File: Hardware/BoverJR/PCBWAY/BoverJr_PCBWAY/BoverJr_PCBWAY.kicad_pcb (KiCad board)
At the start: 2 copper layers, 100 x 100 mm, 55 parts, among them J1 Encoder Derecho, J10 7.4v, J11 Cable_PAD, J2 Encoder Izquierdo, J3 Programador, J4 Distancia_Der, J5 Distancia_Izq, J6 Cable_PAD, J7 Cable_PAD, J8 Distancia_Frontal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

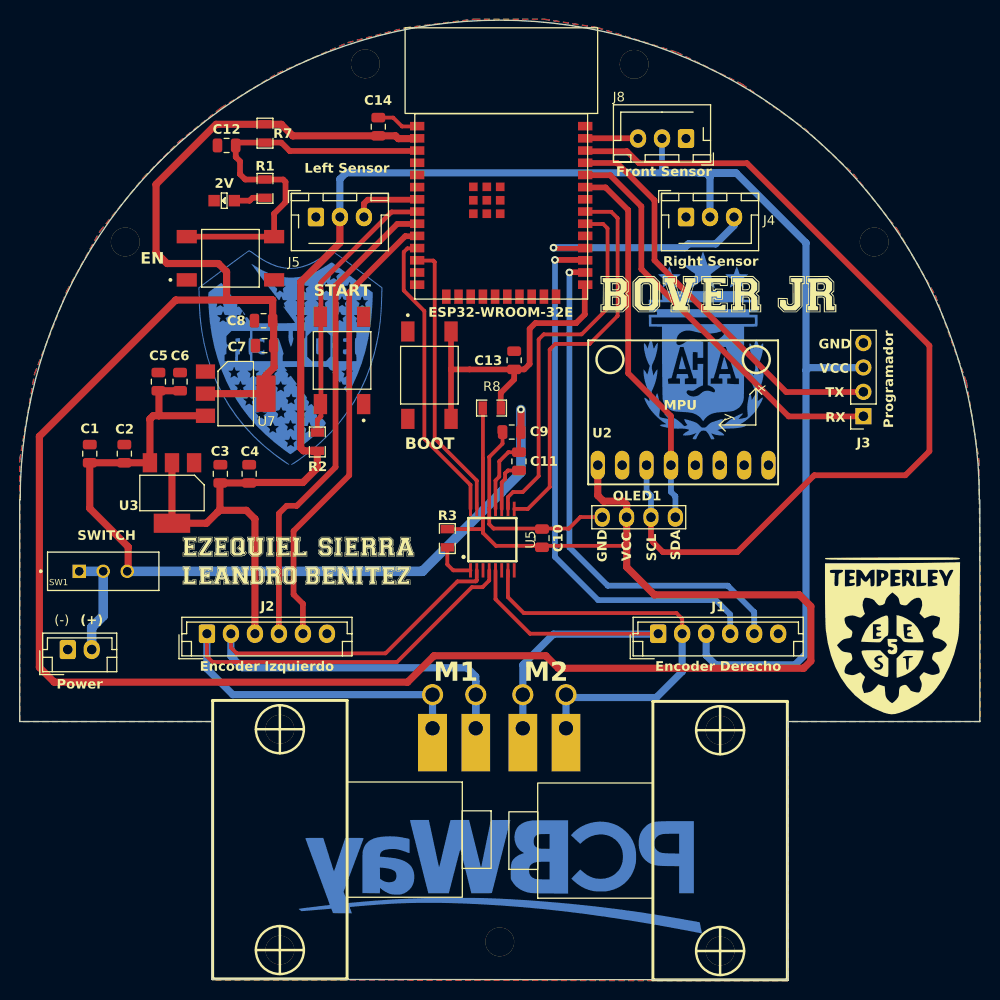
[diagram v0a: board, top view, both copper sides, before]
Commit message: AÑADI BOTON A LABERINTO CHASIS PLACA
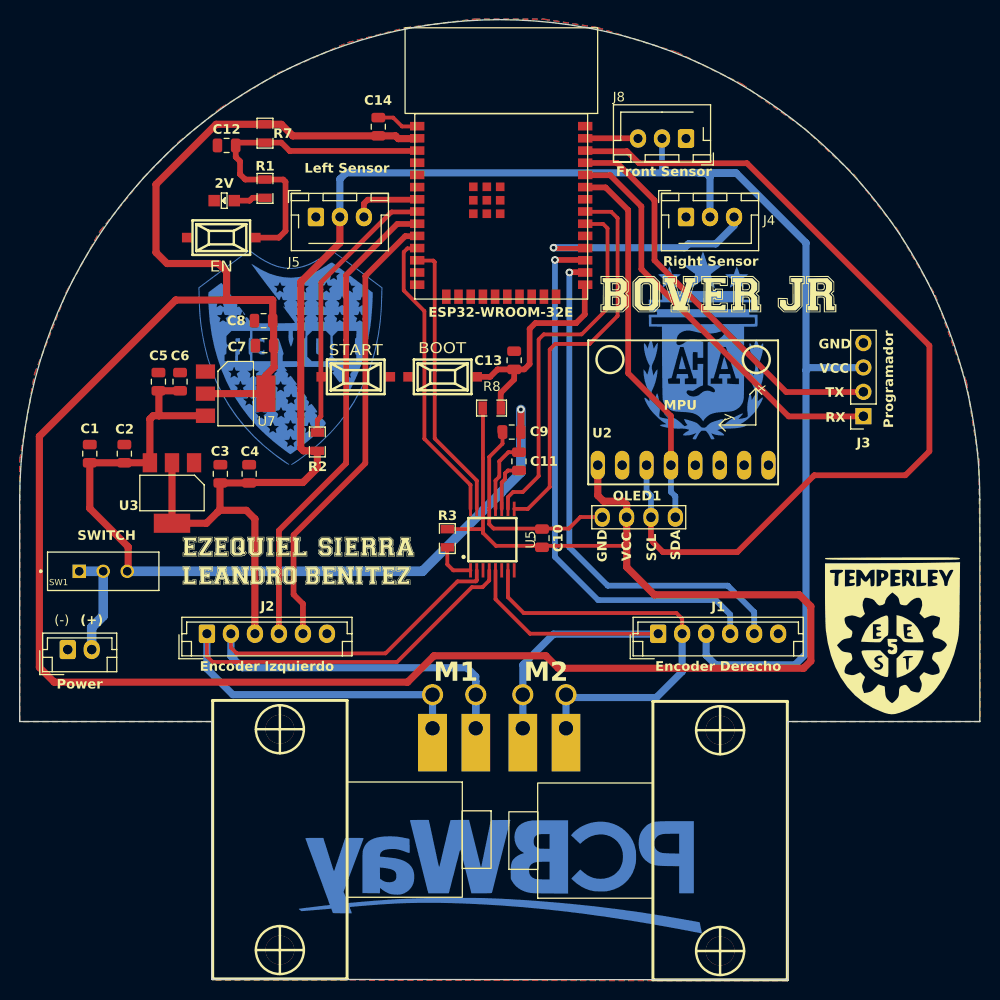
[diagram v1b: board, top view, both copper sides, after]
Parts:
- removed ? (x5): , 
- SW_BOOT1, SW_EN1, SW_START1: footprint EESTN5:SW_TL3301FF160QG -> EESTN5:Pulsador_SMD_2_BAJO
- moved SW_EN1 2.35 mm to (121.0, 52.5)
- moved SW_START1 2.23 mm to (135.0, 67.0), turned to 180 degrees
- moved SW_BOOT1 1.39 mm to (144.1, 67.0), turned to 0 degrees
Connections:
- SW_BOOT1 pad 2: GND -> /BOOT
- SW_EN1 pad 2: GND -> /EN
- SW_START1 pad 2: GND -> /START
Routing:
- net /BOOT: track 35.3 -> 23.8 mm
- net /EN: track 42.9 -> 36.1 mm
- net /OUT_M2_DA: track 50.5 -> 49.9 mm
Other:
- outline, holes or cut-outs redrawn

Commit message: corregi pcb bover JR
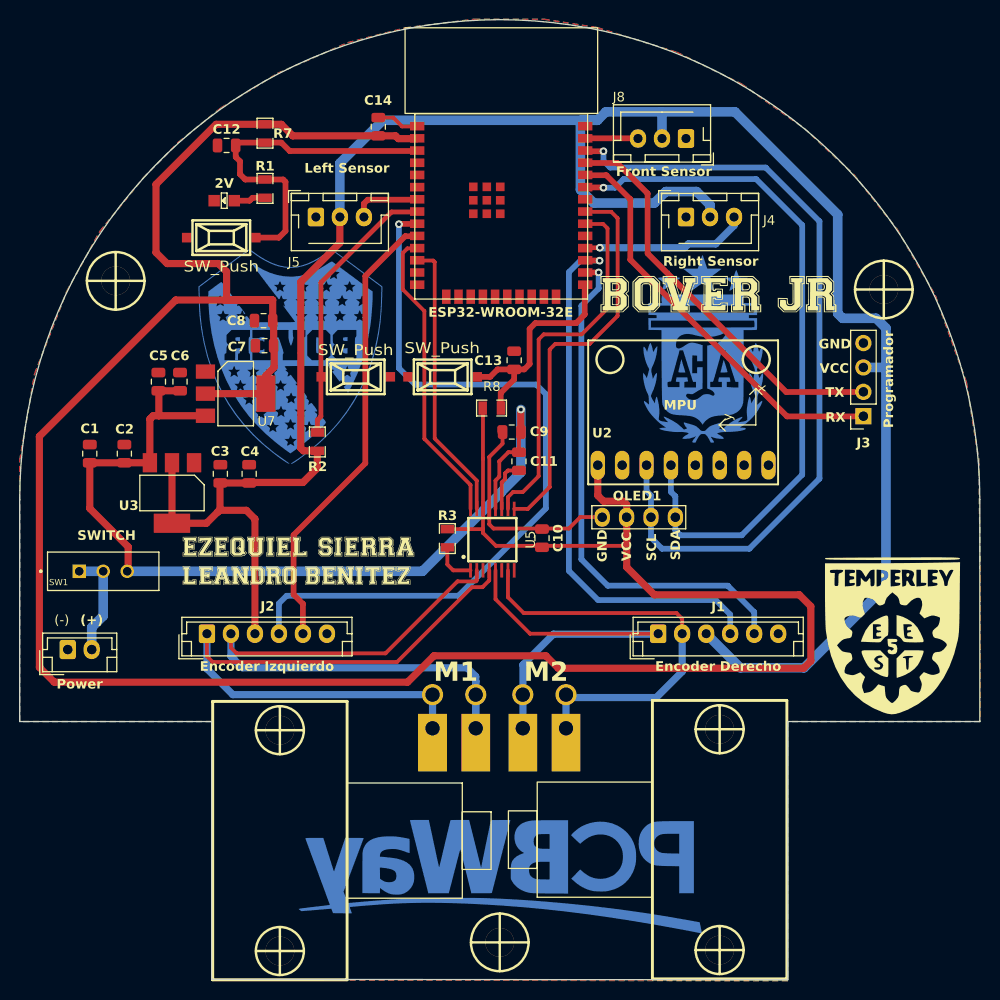
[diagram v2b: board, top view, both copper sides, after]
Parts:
- added H3: Mounting_Hole, EESTN5:hole_3mm, F.Cu at (150.0, 125.9)
- added H4: Mounting_Hole, EESTN5:hole_3mm, F.Cu at (190.0, 57.9)
- added H5: Mounting_Hole, EESTN5:hole_3mm, F.Cu at (110.0, 57.0)
- G2: footprint EESTN5:Bover_Huella_frontal_FCU -> EESTN5:Bover_Huella_BCU_SOLK
- G3: footprint EESTN5:AFA -> EESTN5:AFA_BCU_filks
- SW_BOOT1: value BOOT -> SW_Push
- SW_EN1: value EN -> SW_Push
- SW_START1: value START -> SW_Push
- moved H2 45.8 mm to (127.1, 115.3), turned to -90 degrees
- moved H1 45.8 mm to (172.9, 115.2), turned to 90 degrees
- moved G3 0.35 mm to (171.1, 64.2)
- moved G2 0.10 mm to (128.4, 64.4)
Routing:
- net /SDA: track 39.5 -> 74.0 mm, vias 0 -> 1
- net /OUT_M2_DA: track 49.9 -> 80.3 mm, vias 0 -> 1
- net +5V: track 201.9 -> 232.3 mm
- net /SCL: track 97.1 -> 83.6 mm, vias 0 -> 1
- net /IR_IZQ: track 24.0 -> 17.4 mm

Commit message: laberinto bover JR falta estañar logos
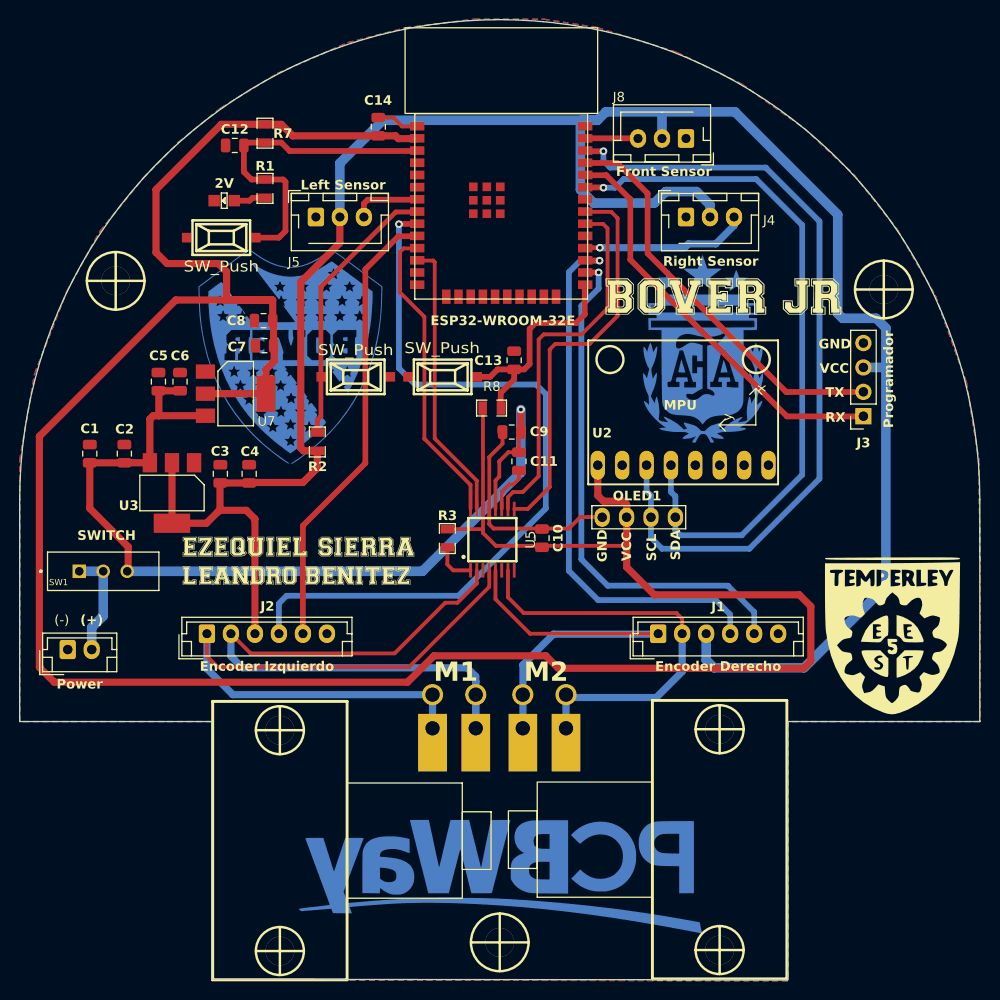
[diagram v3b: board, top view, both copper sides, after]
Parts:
- moved C12 0.85 mm to (122.4, 42.9)
- moved G6 0.58 mm to (173.4, 59.1)
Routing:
- net +5V: track 232.3 -> 233.9 mm
- net /EN: track 36.1 -> 34.6 mm
- net /OUT_A_MOTOR2: track 68.3 -> 69.2 mm
- net /OUT_B_MOTOR2: track 73.4 -> 72.7 mm

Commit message: esperando verificacion de pcbway ya cargue 6 gerber
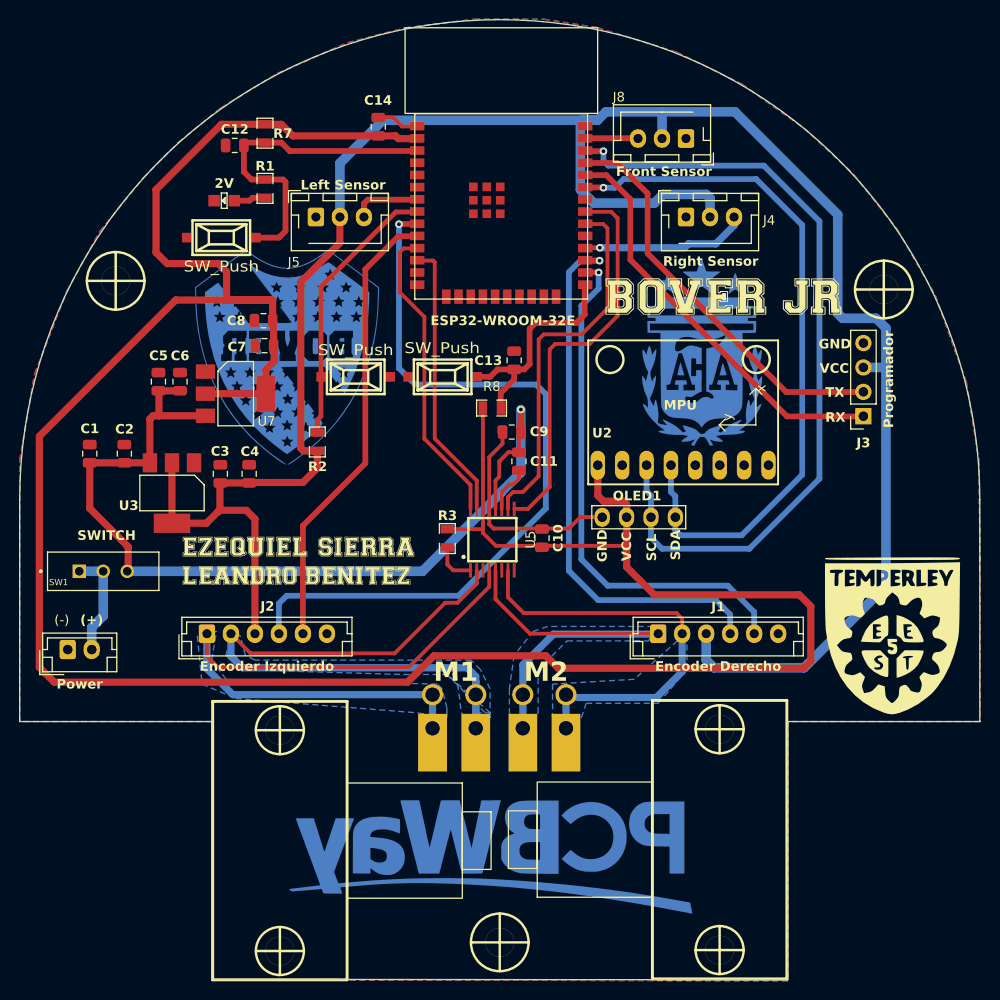
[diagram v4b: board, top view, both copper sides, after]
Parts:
- moved G14 2.28 mm to (148.1, 117.1)
- moved G2 0.36 mm to (128.0, 64.5)
- moved G3 0.32 mm to (171.0, 64.5)
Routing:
- added copper zone on B.Cu, net /OUT_A_MOTOR1
- added copper zone on B.Cu, net /OUT_A_MOTOR2
- added copper zone on B.Cu, net /OUT_B_MOTOR1
- added copper zone on B.Cu, net /OUT_B_MOTOR2
